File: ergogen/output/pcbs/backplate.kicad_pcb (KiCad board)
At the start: 2 copper layers, 117.7 x 96.7 mm, 5 parts

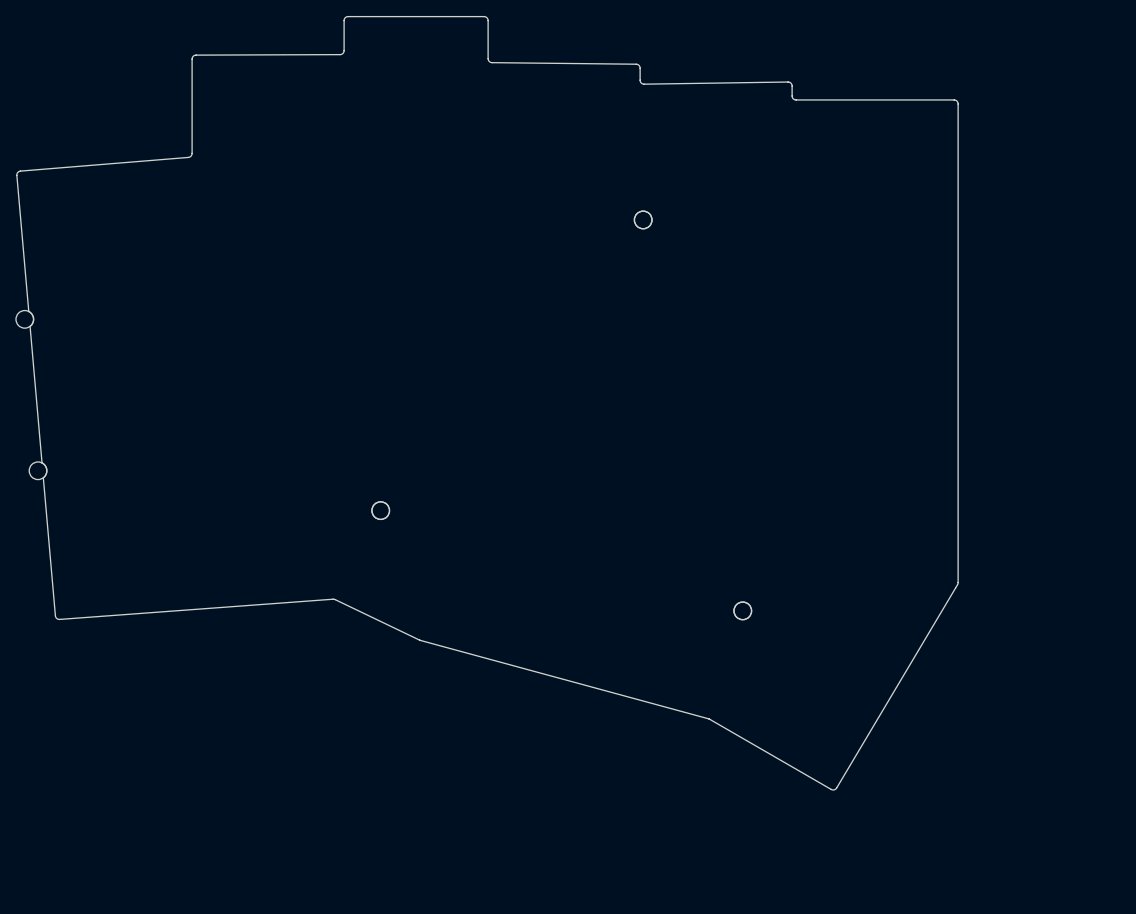
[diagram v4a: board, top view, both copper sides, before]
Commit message: Changed thumb splay
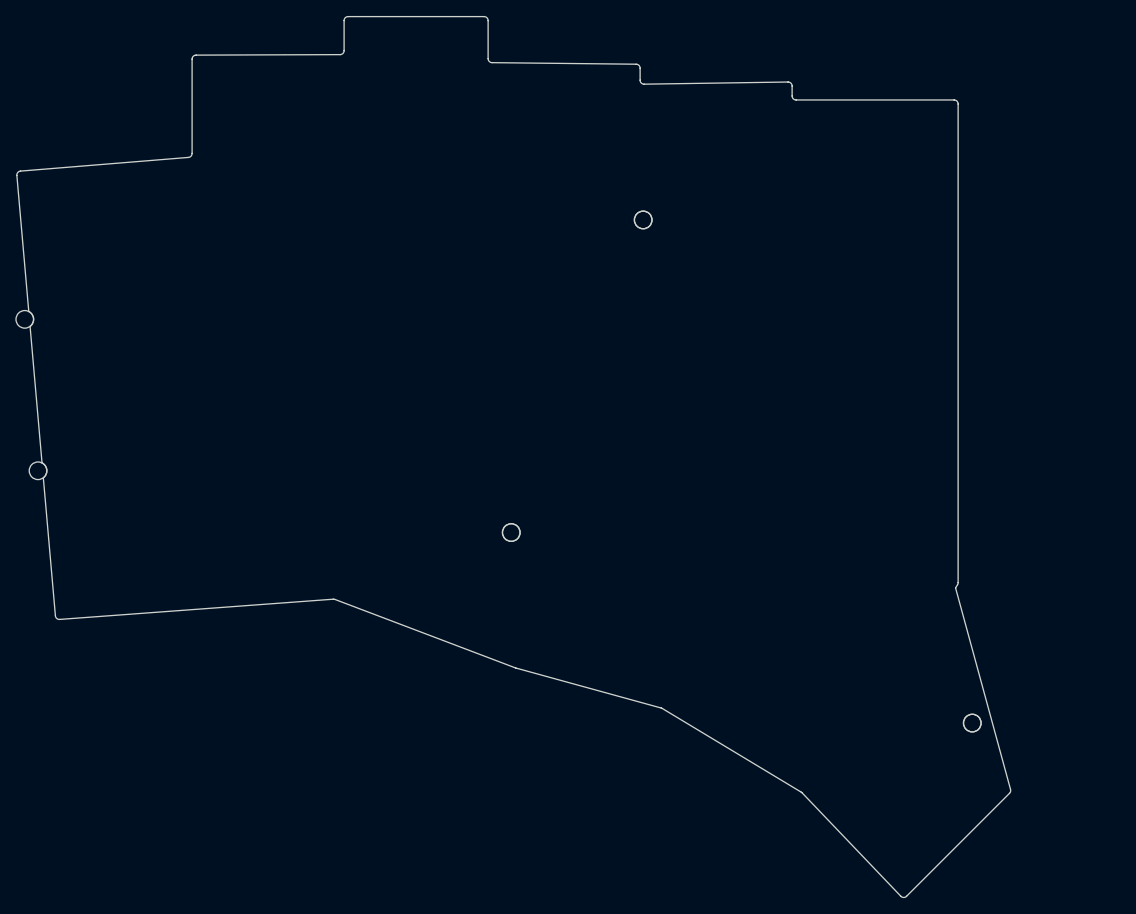
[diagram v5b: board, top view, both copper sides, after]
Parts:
- moved MH5 31.9 mm to (206.5, 122.9), turned to -45 degrees
- moved MH4 16.5 mm to (148.9, 99.1), turned to -15 degrees
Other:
- board size 117.7 x 96.7 mm -> 124.2 x 110.1 mm
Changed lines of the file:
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@@
   )
   (module "ceoloide:mounting_hole_npth" (layer F.Cu)
-      (at 132.541445 96.3445903 0)
-      (fp_text reference "MH4" (at 0 2.55 0) (layer F.SilkS) hide (effects (font (size 1 1) (thickness 0.15))))
-      (pad "" np_thru_hole circle (at 0 0 0) (size 2.2 2.2) (drill 2.2) (layers *.Cu *.Mask))
+      (at 148.8598077 99.0848776 -15)
+      (fp_text reference "MH4" (at 0 2.55 -15) (layer F.SilkS) hide (effects (font (size 1 1) (thickness 0.15))))
+      (pad "" np_thru_hole circle (at 0 0 -15) (size 2.2 2.2) (drill 2.2) (layers *.Cu *.Mask))
   )
   (module "ceoloide:mounting_hole_npth" (layer F.Cu)
-      (at 177.7998255 108.87572 60)
-      (fp_text reference "MH5" (at 0 2.55 60) (layer F.SilkS) hide (effects (font (size 1 1) (thickness 0.15))))
-      (pad "" np_thru_hole circle (at 0 0 60) (size 2.2 2.2) (drill 2.2) (layers *.Cu *.Mask))
+      (at 206.488576 122.90275019999999 -45)
+      (fp_text reference "MH5" (at 0 2.55 -45) (layer F.SilkS) hide (effects (font (size 1 1) (thickness 0.15))))
+      (pad "" np_thru_hole circle (at 0 0 -45) (size 2.2 2.2) (drill 2.2) (layers *.Cu *.Mask))
   )
   (gr_line (start 91.87824460323029 109.49068746980254) (end 90.36871289999999 92.2437231) (layer Edge.Cuts) (stroke (width 0.15) (type default)))
@@
 (gr_line (start 165.47394415076104 43.03997791277865) (end 183.45917122939375 42.77019950801905) (layer Edge.Cuts) (stroke (width 0.15) (type default)))
 (gr_line (start 183.96667038015485 43.26992130873259) (end 183.96722317371228 44.51481240004068) (layer Edge.Cuts) (stroke (width 0.15) (type default)))
-(gr_line (start 204.4024451 106.02118640000002) (end 189.53461200661962 131.01926453205544) (layer Edge.Cuts) (stroke (width 0.15) (type default)))
-(gr_line (start 188.8548751066196 131.19668733205546) (end 173.65217521437296 122.41940443517656) (layer Edge.Cuts) (stroke (width 0.15) (type default)))
-(gr_line (start 173.533396814373 122.36994343517657) (end 137.48845271108377 112.56655937095499) (layer Edge.Cuts) (stroke (width 0.15) (type default)))
-(gr_line (start 137.40332929157933 112.53485706159397) (end 126.84466306000907 107.46728833906015) (layer Edge.Cuts) (stroke (width 0.15) (type default)))
-(gr_line (start 126.59146074050466 107.41942002969911) (end 92.41319770323031 109.94573156980263) (layer Edge.Cuts) (stroke (width 0.15) (type default)))
+(gr_line (start 204.4024451 106.02118640000002) (end 211.26934923259245 131.2007277266382) (layer Edge.Cuts) (stroke (width 0.15) (type default)))
+(gr_line (start 211.1405195199005 131.68583548009948) (end 198.27245950682325 144.55389549317673) (layer Edge.Cuts) (stroke (width 0.15) (type default)))
+(gr_line (start 197.5573001306715 144.5456552181502) (end 185.2184018103768 131.6245719172887) (layer Edge.Cuts) (stroke (width 0.15) (type default)))
+(gr_line (start 185.11474537091743 131.54156036435938) (end 167.73632242747522 121.07577102297391) (layer Edge.Cuts) (stroke (width 0.15) (type default)))
+(gr_line (start 167.61101352447525 121.02201021014679) (end 149.42297909295323 116.01776895205687) (layer Edge.Cuts) (stroke (width 0.15) (type default)))
+(gr_line (start 149.37827902664569 116.003177061327) (end 126.82809141312292 107.44890800214452) (layer Edge.Cuts) (stroke (width 0.15) (type default)))
+(gr_line (start 126.61389341312291 107.4177619021445) (end 92.41319770323031 109.94573156980263) (layer Edge.Cuts) (stroke (width 0.15) (type default)))
 (gr_line (start 184.46722317371226 45.01459040000001) (end 204.2174451 45.01459040000001) (layer Edge.Cuts) (stroke (width 0.15) (type default)))
 (gr_line (start 204.7174451 45.51459040000001) (end 204.7174451 105.34161580612954) (layer Edge.Cuts) (stroke (width 0.15) (type default)))
@@
 (gr_arc (start 204.7174451 45.51459040000001) (mid 204.5709985 45.16103700000001) (end 204.2174451 45.01459040000001) (layer Edge.Cuts) (stroke (width 0.15) (type default)))
 (gr_arc (start 204.6504578 105.59161580612954) (mid 204.70040799999998 105.47102530612953) (end 204.7174451 105.34161580612954) (layer Edge.Cuts) (stroke (width 0.15) (type default)))
-(gr_arc (start 188.8548751066196 131.1966873320555) (mid 189.2311528066196 131.2474658320555) (end 189.5346120066196 131.01926453205547) (layer Edge.Cuts) (stroke (width 0.15) (type default)))
-(gr_arc (start 173.65217521437296 122.41940443517656) (mid 173.59438361437296 122.39083733517657) (end 173.53339681437296 122.36994343517657) (layer Edge.Cuts) (stroke (width 0.15) (type default)))
-(gr_arc (start 137.40332931108378 112.534857070955) (mid 137.44516961108377 112.55264527095501) (end 137.48845271108377 112.566559370955) (layer Edge.Cuts) (stroke (width 0.15) (type default)))
-(gr_arc (start 126.84466304050464 107.46728832969912) (mid 126.72119864050464 107.42676222969911) (end 126.59146074050464 107.41942002969911) (layer Edge.Cuts) (stroke (width 0.15) (type default)))
+(gr_arc (start 211.14051951990052 131.6858354800995) (mid 211.27021541990052 131.4606182800995) (end 211.2693492199005 131.2007276800995) (layer Edge.Cuts) (stroke (width 0.15) (type default)))
+(gr_arc (start 197.55730020682324 144.5456551931767) (mid 197.91314540682325 144.70030889317673) (end 198.27245950682325 144.5538953931767) (layer Edge.Cuts) (stroke (width 0.15) (type default)))
+(gr_arc (start 185.21840173422504 131.62457194226215) (mid 185.16934173422504 131.57960944226215) (end 185.11474533422503 131.54156034226216) (layer Edge.Cuts) (stroke (width 0.15) (type default)))
+(gr_arc (start 167.7363223907828 121.07577100087666) (mid 167.6755091907828 121.04459890087666) (end 167.6110134907828 121.02201020087666) (layer Edge.Cuts) (stroke (width 0.15) (type default)))
+(gr_arc (start 149.37827902664569 116.003177061327) (mid 149.4004574266457 116.010998761327) (end 149.42297912664569 116.017768961327) (layer Edge.Cuts) (stroke (width 0.15) (type default)))
+(gr_arc (start 126.8280914131229 107.4489080021445) (mid 126.72269801312291 107.4216051021445) (end 126.61389341312291 107.4177619021445) (layer Edge.Cuts) (stroke (width 0.15) (type default)))
 (gr_arc (start 91.8782446032303 109.49068746980264) (mid 92.0523782032303 109.82794416980263) (end 92.4131977032303 109.94573156980263) (layer Edge.Cuts) (stroke (width 0.15) (type default)))
 (gr_arc (start 88.71211749999999 73.3165013) (mid 89.14802249999998 72.3405203) (end 88.54919959999998 71.4551034) (layer Edge.Cuts) (stroke (width 0.15) (type default)))
 (gr_arc (start 90.36871289999999 92.2437231) (mid 90.80398159999999 91.2682196) (end 90.2058682 90.3831623) (layer Edge.Cuts) (stroke (width 0.15) (type default)))
 (gr_circle (center 165.35244509999998 60.01059040000001) (end 166.45244509999998 60.01059040000001) (layer Edge.Cuts) (stroke (width 0.15) (type default)) (fill none))
-(gr_circle (center 132.541445 96.3445903) (end 133.641445 96.3445903) (layer Edge.Cuts) (stroke (width 0.15) (type default)) (fill none))
-(gr_circle (center 177.7998255 108.87572) (end 178.8998255 108.87572) (layer Edge.Cuts) (stroke (width 0.15) (type default)) (fill none))
+(gr_circle (center 148.8598077 99.0848776) (end 149.9598077 99.0848776) (layer Edge.Cuts) (stroke (width 0.15) (type default)) (fill none))
+(gr_circle (center 206.488576 122.90275019999999) (end 207.588576 122.90275019999999) (layer Edge.Cuts) (stroke (width 0.15) (type default)) (fill none))
 )

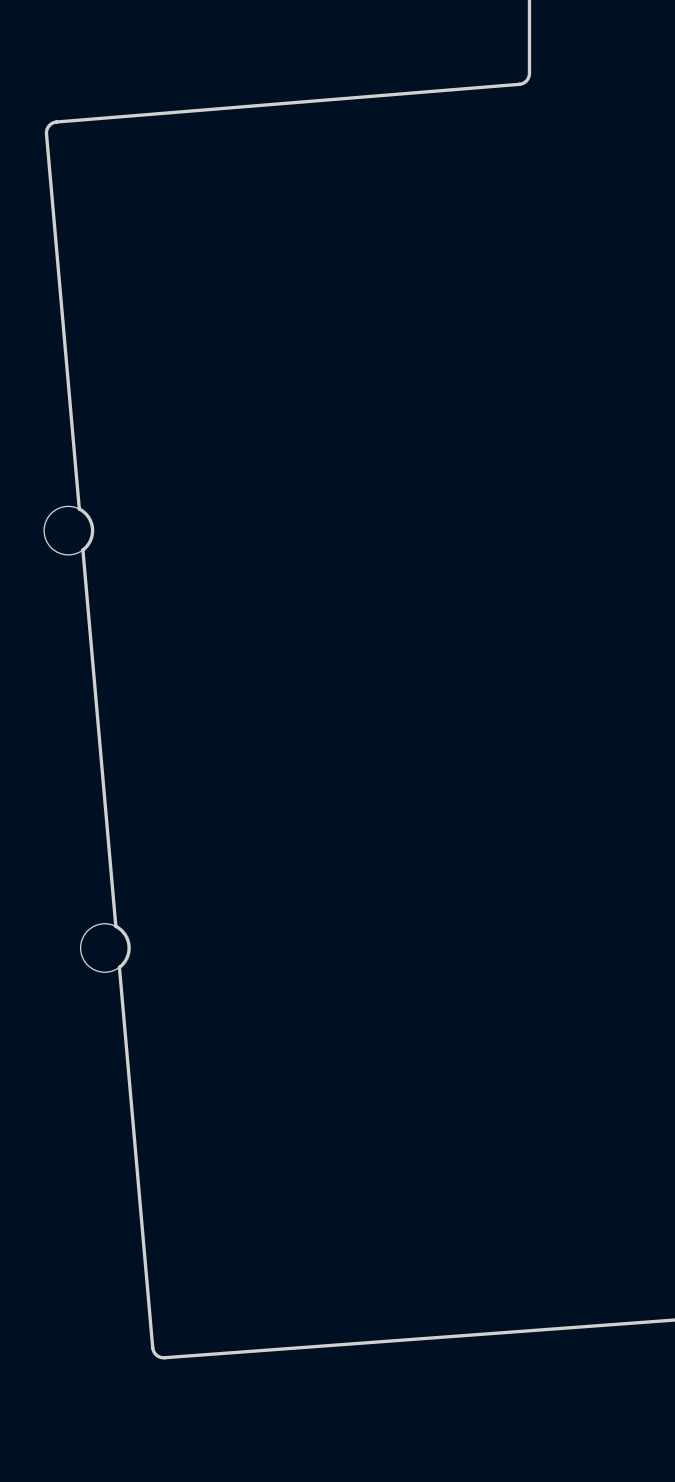
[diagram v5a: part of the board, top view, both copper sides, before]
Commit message: Moved screws back onto board
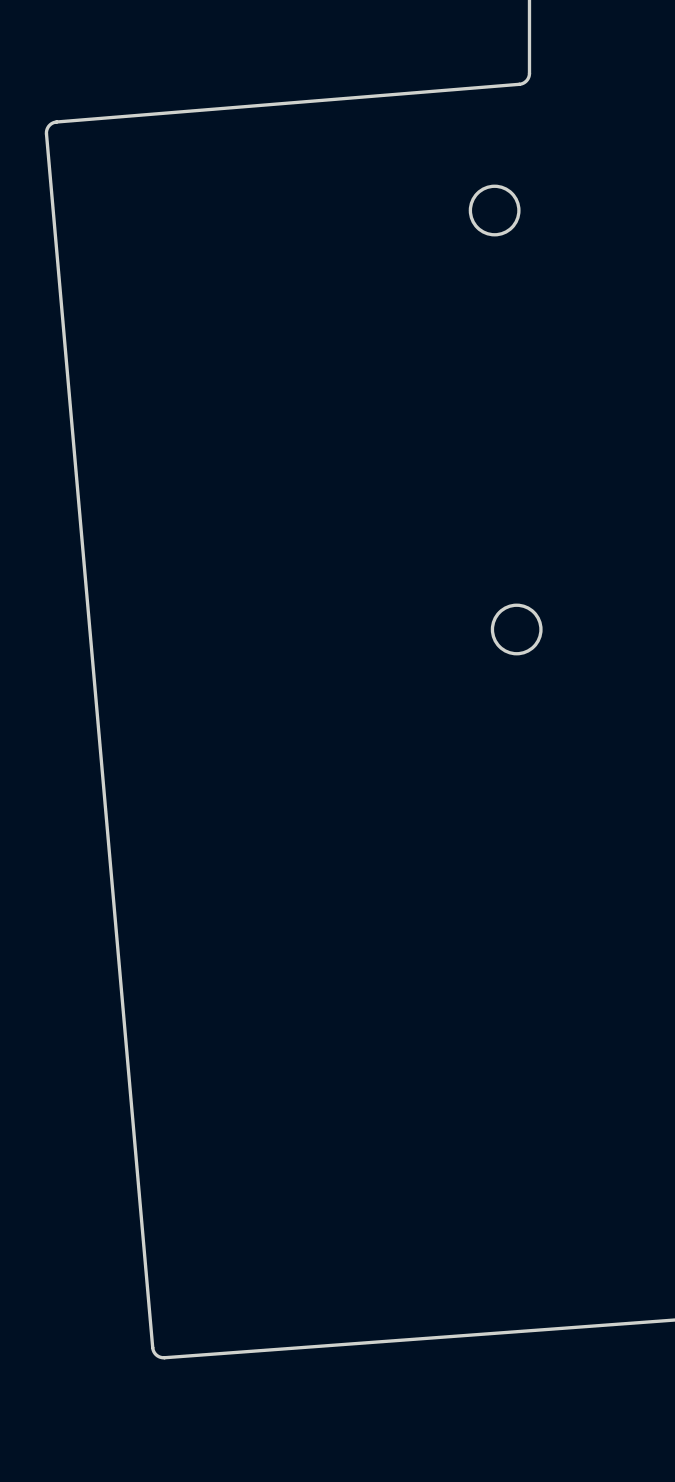
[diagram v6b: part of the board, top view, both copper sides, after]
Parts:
- moved MH1 24.2 mm to (107.4, 57.9), turned to 0 degrees
- moved MH2 23.6 mm to (108.4, 76.9), turned to 0 degrees
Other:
- outline, holes or cut-outs redrawn
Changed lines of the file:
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@@
   (net 0 "")
   (module "ceoloide:mounting_hole_npth" (layer F.Cu)
-      (at 88.05221169999999 72.4364306 5)
-      (fp_text reference "MH1" (at 0 2.55 5) (layer F.SilkS) hide (effects (font (size 1 1) (thickness 0.15))))
-      (pad "" np_thru_hole circle (at 0 0 5) (size 2.2 2.2) (drill 2.2) (layers *.Cu *.Mask))
+      (at 107.384445 57.919590400000004 0)
+      (fp_text reference "MH1" (at 0 2.55 0) (layer F.SilkS) hide (effects (font (size 1 1) (thickness 0.15))))
+      (pad "" np_thru_hole circle (at 0 0 0) (size 2.2 2.2) (drill 2.2) (layers *.Cu *.Mask))
   )
   (module "ceoloide:mounting_hole_npth" (layer F.Cu)
-      (at 89.70817079999999 91.3641299 5)
-      (fp_text reference "MH2" (at 0 2.55 5) (layer F.SilkS) hide (effects (font (size 1 1) (thickness 0.15))))
-      (pad "" np_thru_hole circle (at 0 0 5) (size 2.2 2.2) (drill 2.2) (layers *.Cu *.Mask))
+      (at 108.384445 76.9195904 0)
+      (fp_text reference "MH2" (at 0 2.55 0) (layer F.SilkS) hide (effects (font (size 1 1) (thickness 0.15))))
+      (pad "" np_thru_hole circle (at 0 0 0) (size 2.2 2.2) (drill 2.2) (layers *.Cu *.Mask))
   )
   (module "ceoloide:mounting_hole_npth" (layer F.Cu)
@@
       (pad "" np_thru_hole circle (at 0 0 -45) (size 2.2 2.2) (drill 2.2) (layers *.Cu *.Mask))
   )
-  (gr_line (start 91.87824460323029 109.49068746980254) (end 90.36871289999999 92.2437231) (layer Edge.Cuts) (stroke (width 0.15) (type default)))
-(gr_line (start 88.54919959999998 71.4551034) (end 87.06061104775414 54.447423555018986) (layer Edge.Cuts) (stroke (width 0.15) (type default)))
-(gr_line (start 90.2058682 90.38316239999999) (end 88.71211749999999 73.3165013) (layer Edge.Cuts) (stroke (width 0.15) (type default)))
+  (gr_line (start 91.87824460323029 109.49068746980254) (end 87.06061104775414 54.447423555018986) (layer Edge.Cuts) (stroke (width 0.15) (type default)))
 (gr_line (start 87.51811429808367 53.90547845906503) (end 108.50503754967045 52.19601094528491) (layer Edge.Cuts) (stroke (width 0.15) (type default)))
 (gr_line (start 108.964445 51.69766144933076) (end 108.964445 39.90788282277217) (layer Edge.Cuts) (stroke (width 0.15) (type default)))
@@
 (gr_arc (start 126.8280914131229 107.4489080021445) (mid 126.72269801312291 107.4216051021445) (end 126.61389341312291 107.4177619021445) (layer Edge.Cuts) (stroke (width 0.15) (type default)))
 (gr_arc (start 91.8782446032303 109.49068746980264) (mid 92.0523782032303 109.82794416980263) (end 92.4131977032303 109.94573156980263) (layer Edge.Cuts) (stroke (width 0.15) (type default)))
-(gr_arc (start 88.71211749999999 73.3165013) (mid 89.14802249999998 72.3405203) (end 88.54919959999998 71.4551034) (layer Edge.Cuts) (stroke (width 0.15) (type default)))
-(gr_arc (start 90.36871289999999 92.2437231) (mid 90.80398159999999 91.2682196) (end 90.2058682 90.3831623) (layer Edge.Cuts) (stroke (width 0.15) (type default)))
+(gr_circle (center 107.384445 57.919590400000004) (end 108.484445 57.919590400000004) (layer Edge.Cuts) (stroke (width 0.15) (type default)) (fill none))
+(gr_circle (center 108.384445 76.9195904) (end 109.484445 76.9195904) (layer Edge.Cuts) (stroke (width 0.15) (type default)) (fill none))
 (gr_circle (center 165.35244509999998 60.01059040000001) (end 166.45244509999998 60.01059040000001) (layer Edge.Cuts) (stroke (width 0.15) (type default)) (fill none))
 (gr_circle (center 148.8598077 99.0848776) (end 149.9598077 99.0848776) (layer Edge.Cuts) (stroke (width 0.15) (type default)) (fill none))
